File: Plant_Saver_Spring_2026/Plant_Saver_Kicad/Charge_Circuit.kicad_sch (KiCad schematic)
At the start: 16 parts, among them J1 1.25mm, Q1 SSF1341, Q3 SSF1341, Q4 SSF1341, Q5 SSF1341, Q6 SSF1341, Q7 SSF1341, Q8 SSF1341, Q9 SSF1341

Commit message: Sensor Fun
Had to annotate in order to assign footprints, If that messed anything up I'd be happy to fix it. Added a basic 1x4 header for the temp sensor and added the correct female pins/header footprint for the capacitive moisture sensor. Also put a footprint in there for the OLED using the 4pin cable that we don't have but would be nice to. If we choose to go with the headers instead it's and easy change.
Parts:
- CR1: footprint SDO_CFP5_SOD128_NEX -> (none)
- J1: footprint CONN02_530470210_MOL -> (none)
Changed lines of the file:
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@@
 			)
 		)
-		(property "Footprint" "CONN02_530470210_MOL"
+		(property "Footprint" ""
 			(at 185.42 120.65 0)
 			(effects
@@
 			)
 		)
-		(property "Footprint" "SDO_CFP5_SOD128_NEX"
+		(property "Footprint" ""
 			(at 217.17 91.44 0)
 			(effects

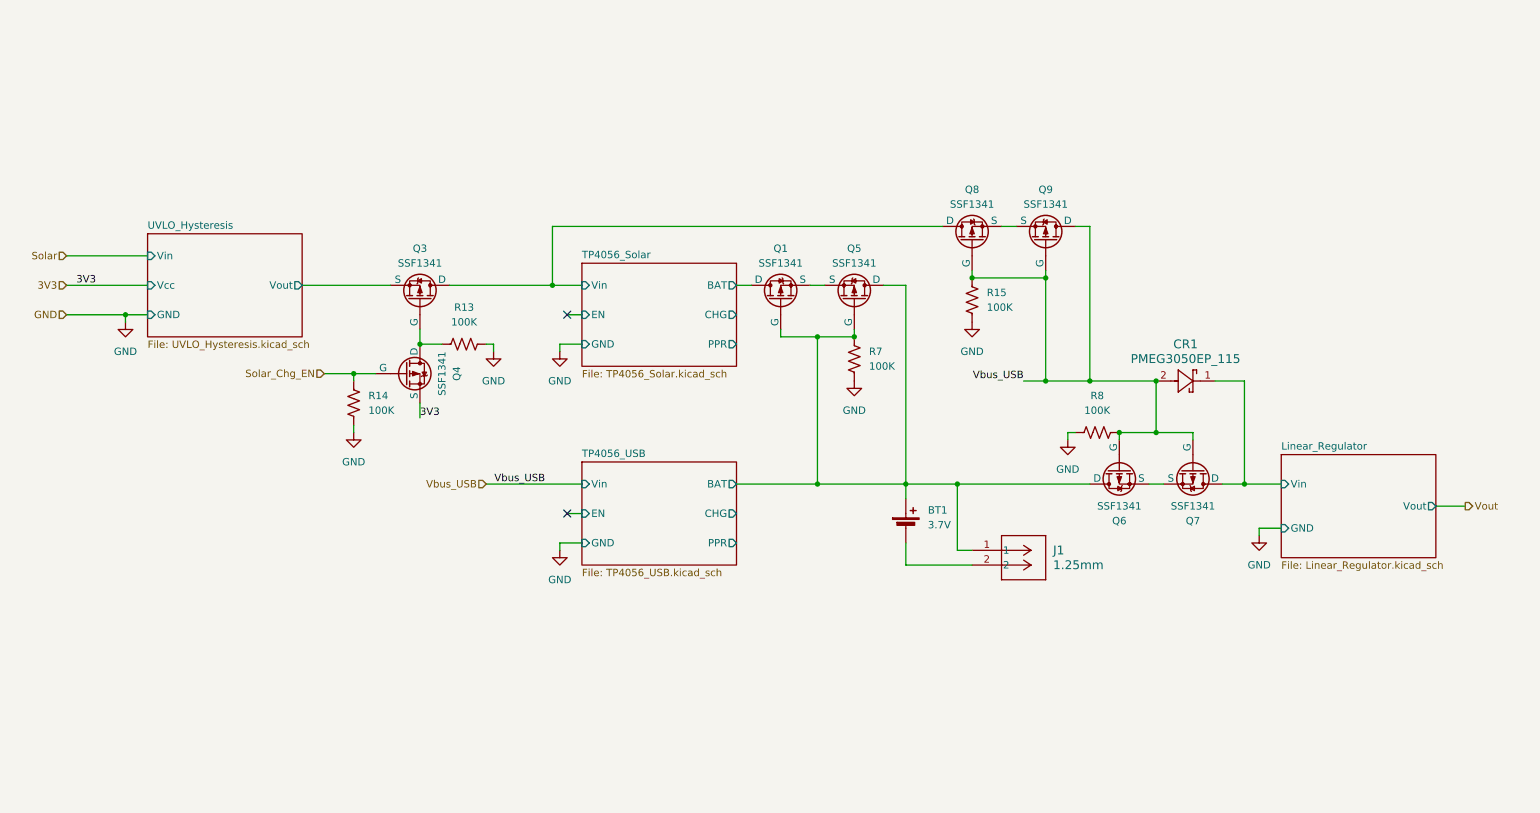
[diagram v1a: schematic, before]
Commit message: Updated Charging Circuit
Replaced TP4056 with MCP73833, replaced schottky diodes
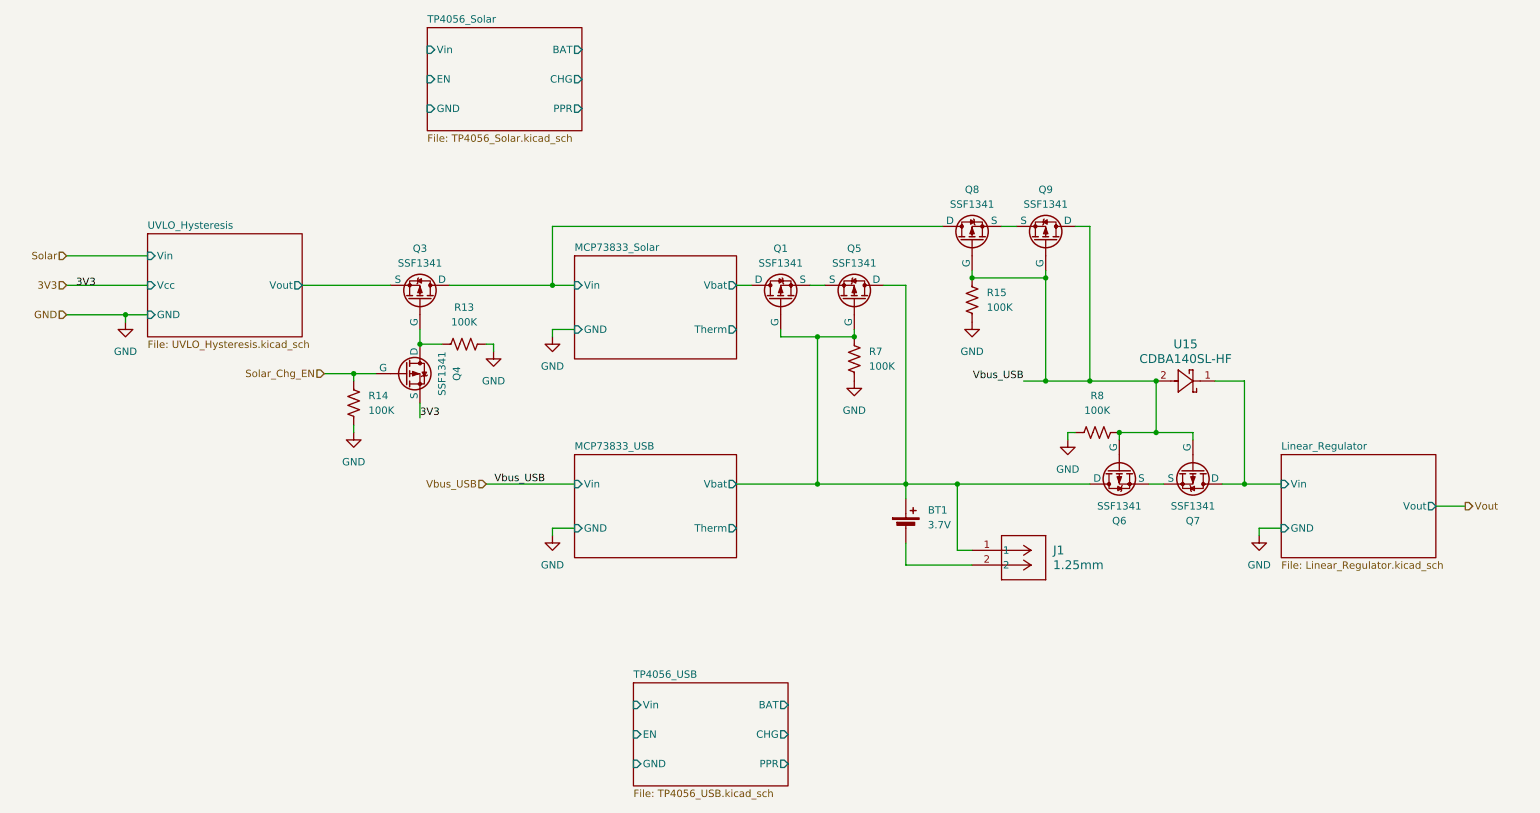
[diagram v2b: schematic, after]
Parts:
- removed CR1: PMEG3050EP_115, symbol PMEG3050EP,115:PMEG3050EP_115
- added U15: CDBA140SL-HF, CDBA-HF, symbol CDBA140SL_HF:CDBA140SL-HF
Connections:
- net Linear_Regulator/Vin: now also U15.1
- net TP4056_Solar/BAT: no longer Q1.1 (D)
- net TP4056_Solar/Vin: no longer Q3.1 (D), Q8.1 (D)
- net TP4056_USB/BAT: no longer BT1.1 (+), J1.1, Q1.2 (G), Q5.1 (D), Q5.2 (G), Q6.1 (D), R7.2
- net Vbus_USB: now also U15.2
- new net MCP73833_Solar/Vbat: Q1.1 (D)
- new net MCP73833_Solar/Vin: Q3.1 (D), Q8.1 (D)
- new net MCP73833_USB/Vbat: BT1.1 (+), J1.1, Q1.2 (G), Q5.1 (D), Q5.2 (G), Q6.1 (D), R7.2
- no-connect marks 2 -> 0
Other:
- added sheet MCP73833_Solar (MCP73833_Solar.kicad_sch)
- added sheet MCP73833_USB (MCP73833_USB.kicad_sch)

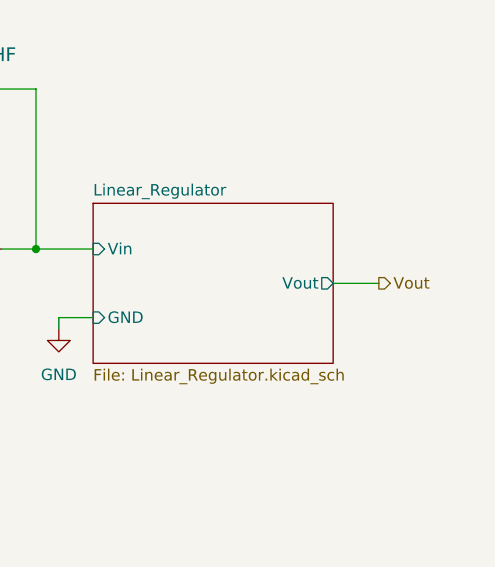
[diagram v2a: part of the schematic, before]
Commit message: Added ESP32 micro and mostly completed its wiring to peripherals
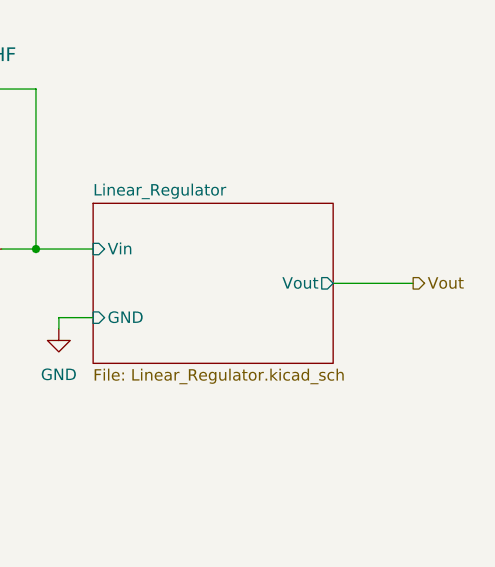
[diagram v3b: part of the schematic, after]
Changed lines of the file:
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@@
 	(wire
 		(pts
-			(xy 265.43 113.03) (xy 270.51 113.03)
+			(xy 265.43 113.03) (xy 274.32 113.03)
 		)
 		(stroke
@@
 	(hierarchical_label "Vout"
 		(shape output)
-		(at 270.51 113.03 0)
+		(at 274.32 113.03 0)
 		(effects
 			(font

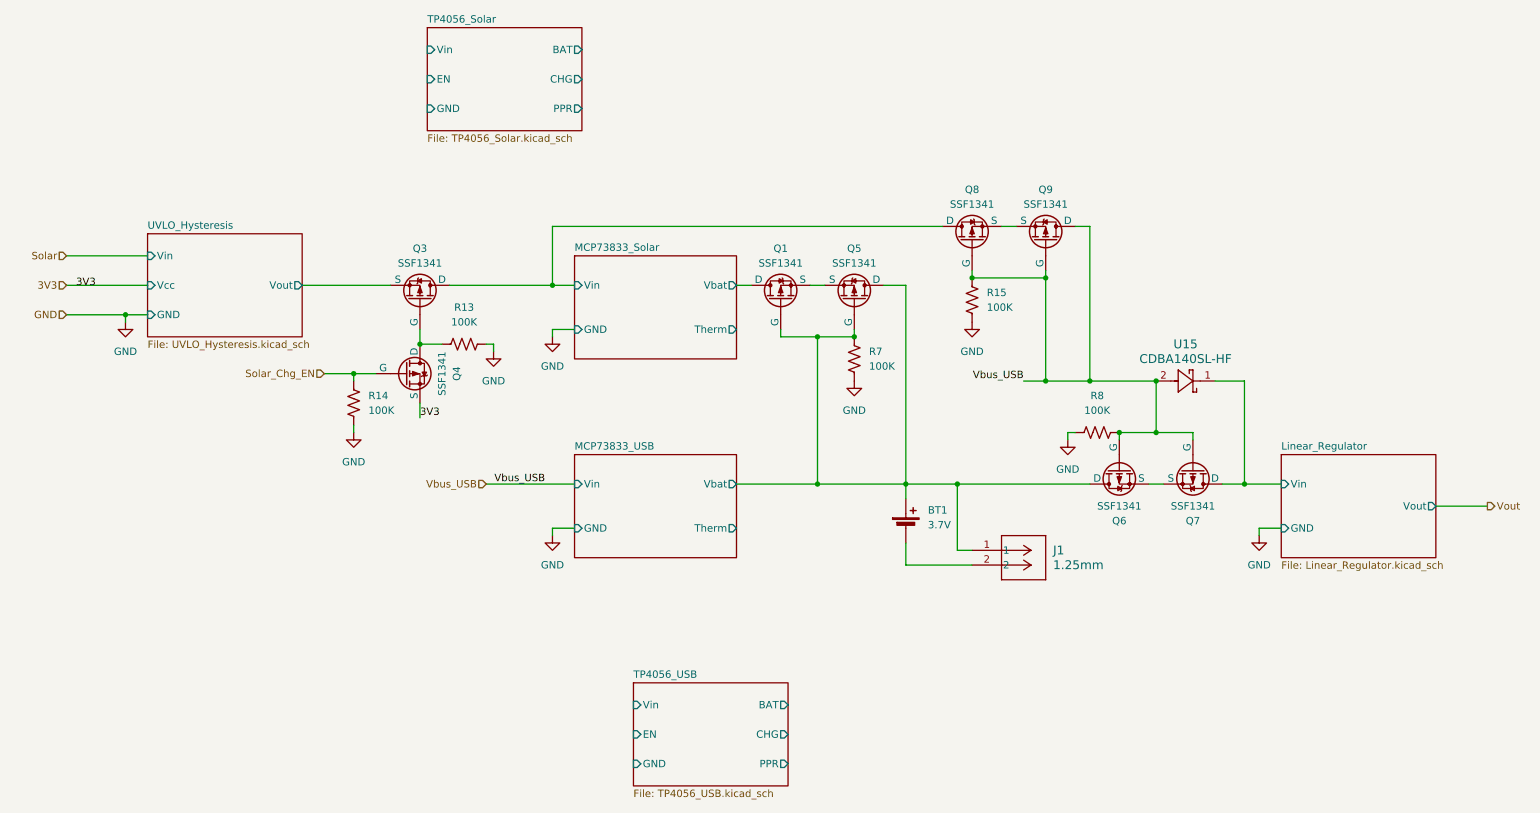
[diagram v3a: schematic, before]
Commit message: Updates to power schematic
Replaced certain selection transistors for lower Rds_on, added thermal cutoff and DW03 for battery protection, swapped in 4-channel op-amps for solar measurement, various misc. improvements.
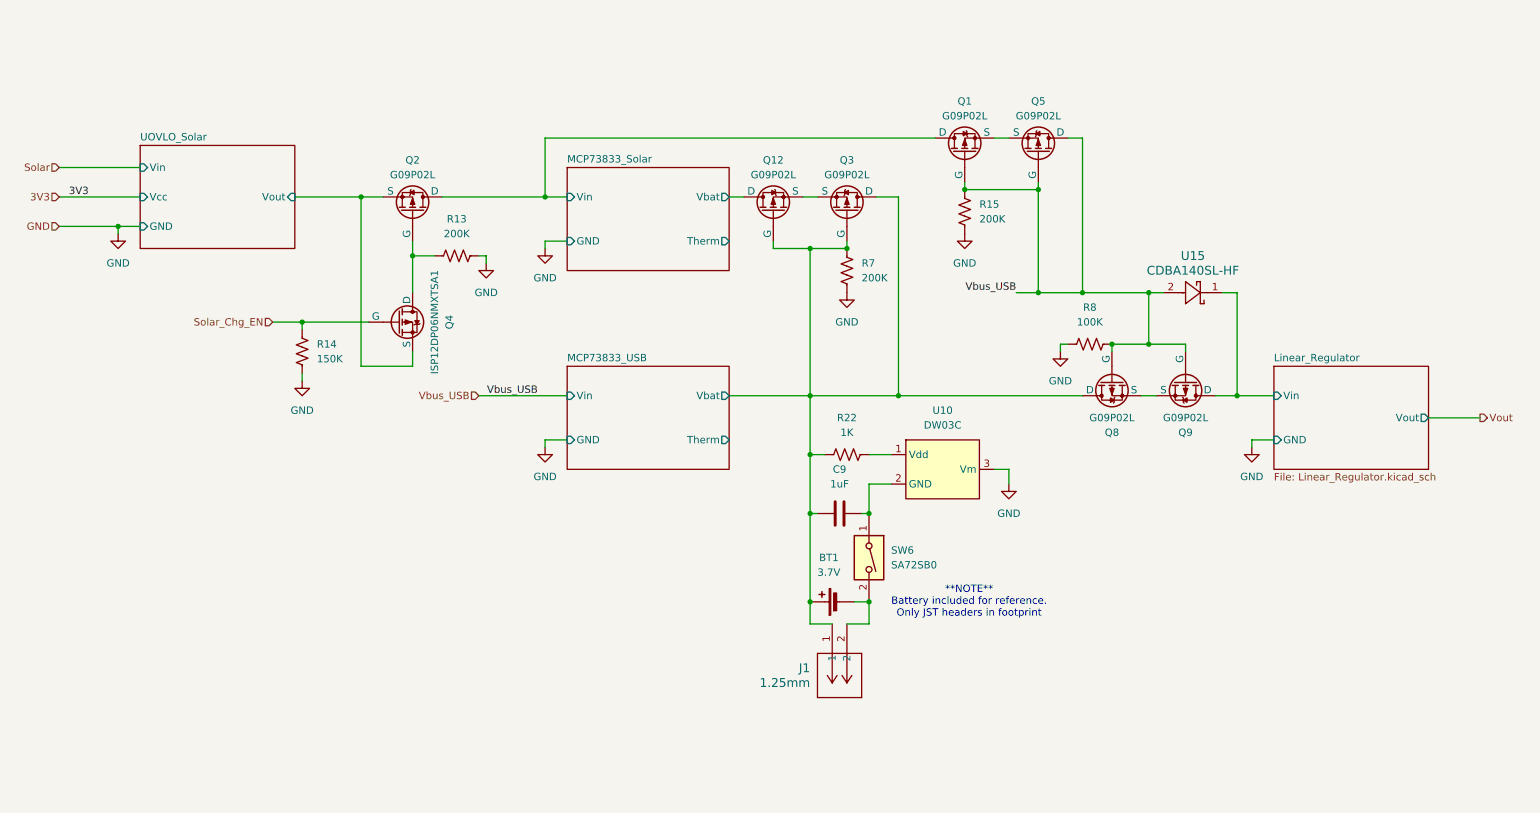
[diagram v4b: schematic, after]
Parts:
- removed Q6, Q7: SSF1341, Package_TO_SOT_SMD:SOT-23_Handsoldering, symbol Simulation_SPICE:PMOS
- added C9: 1uF, C410C105K5R5TA7200:CAP_C410C_AX_X7R_AXIMAX_KEM, symbol Device:C
- added Q12, Q2: G09P02L, G09P02L:TSOT-23, symbol Simulation_SPICE:PMOS
- added R22: 1K, Resistor_THT:R_Axial_DIN0207_L6.3mm_D2.5mm_P10.16mm_Horizontal, symbol Device:R_US
- added SW6: SA72SB0, Resistor_THT:R_Axial_DIN0207_L6.3mm_D2.5mm_P10.16mm_Horizontal, symbol Switch:SW_DIP_x01
- added U10: DW03C, symbol DW03C:_1
- J1: footprint (none) -> 1.25mm Micro-JST Male:CONN02_530470210_MOL
- Q1, Q3, Q5, Q8, Q9: value SSF1341 -> G09P02L; footprint Package_TO_SOT_SMD:SOT-23_Handsoldering -> G09P02L:TSOT-23
- Q4: value SSF1341 -> ISP12DP06NMXTSA1; footprint Package_TO_SOT_SMD:SOT-23_Handsoldering -> ul_ISP12DP06NMXTSA1:PG-SOT223-4_INF
- R13, R15, R7: value 100K -> 200K
- R14: value 100K -> 150K
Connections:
- net 3V3: no longer Q4.3 (S)
- net GND: now also U10.3 (Vm)
- net Linear_Regulator/Vin: now also Q9.1 (D)
- net MCP73833_Solar/Vbat: now also Q12.1 (D); no longer Q1.1 (D)
- net MCP73833_Solar/Vin: now also Q1.1 (D), Q2.1 (D); no longer Q3.1 (D), Q8.1 (D)
- net MCP73833_USB/Vbat: now also Q3.1 (D), Q3.2 (G), Q8.1 (D), C9.1, Q12.2 (G), R22.1; no longer Q1.2 (G), Q5.1 (D), Q5.2 (G)
- net Vbus_USB: now also Q1.2 (G), Q5.1 (D), Q5.2 (G); no longer Q9.1 (D)
- net at Q4.1 (D), R13.1: now also Q2.2 (G); no longer Q3.2 (G)
- net at BT1.2 (-), J1.2: now also SW6.2
- net UVLO_Hysteresis/Vout: no longer names the net of Q3.3 (S)
- net UVLO_Hysteresis/Vout: now also Q12.3 (S)
- new net: R22.2, U10.1 (Vdd)
- new net: C9.2, SW6.1, U10.2 (GND)
- new net UOVLO_Solar/Vout: Q2.3 (S), Q4.3 (S)
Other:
- removed sheet TP4056_Solar
- removed sheet TP4056_USB
- removed sheet UVLO_Hysteresis
- added sheet UOVLO_Solar (UOVLO_Solar.kicad_sch)
- note added: "**NOTE** Battery included for reference. Only JST headers in footprint"
- moved on the sheet: J1, Q4, R13, R14, R15, R7, R8, U15

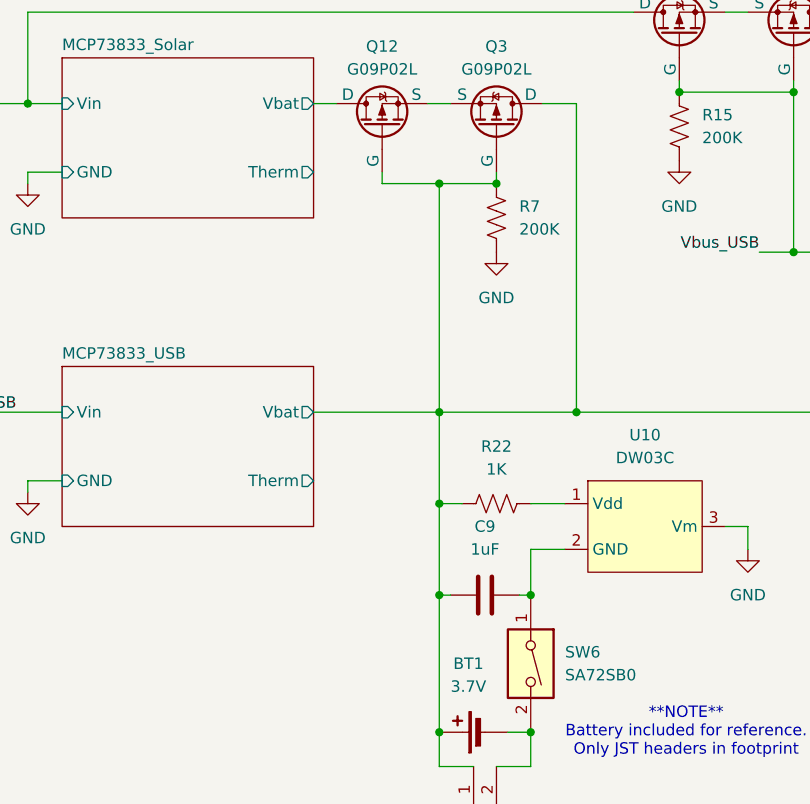
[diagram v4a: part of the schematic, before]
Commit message: Schematic updates
Added USB charge LEDs, updated PMOS gates, added micro connections and revised some of the charging set up.
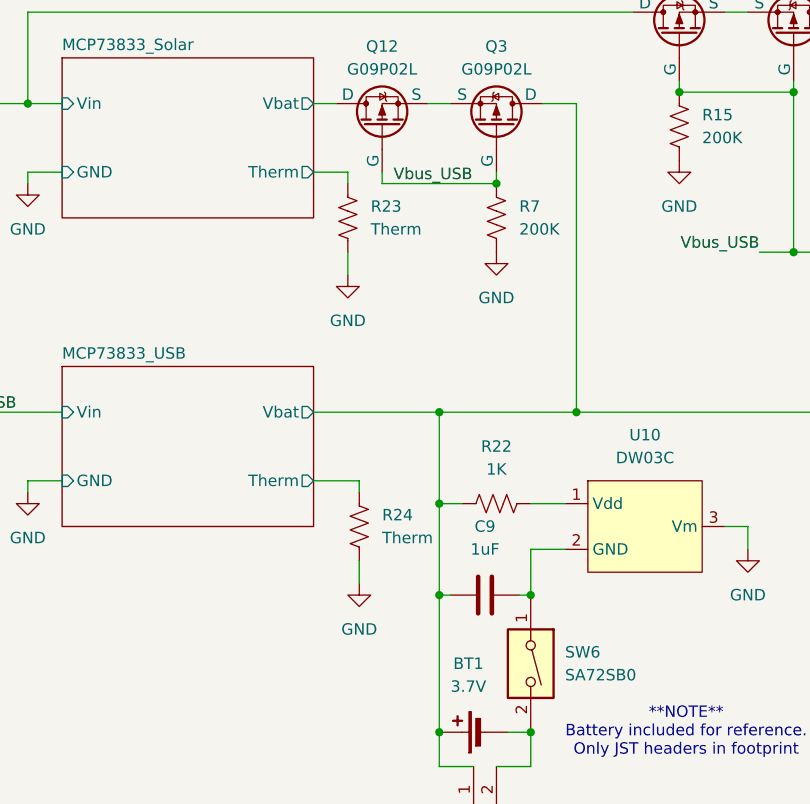
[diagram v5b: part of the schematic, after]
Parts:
- added R23, R24: Therm, Resistor_THT:R_Axial_DIN0207_L6.3mm_D2.5mm_P10.16mm_Horizontal, symbol Device:R_US
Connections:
- net GND: now also R23.1, R24.1
- net MCP73833_Solar/Therm: now also R23.2
- net MCP73833_USB/Therm: now also R24.2
- net MCP73833_USB/Vbat: no longer Q12.2 (G), Q3.2 (G), R7.2
- net Vbus_USB: now also Q12.2 (G), Q3.2 (G), R7.2

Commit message: Minor updates to charge/power
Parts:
- added U11: CDBA140SL-HF, CDBA-HF, symbol CDBA140SL_HF:CDBA140SL-HF
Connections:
- net Vbus_USB: now also U11.2; no longer Q5.1 (D), Q8.2 (G), Q9.2 (G), R8.1, U15.2
- new net: Q5.1 (D), Q8.2 (G), Q9.2 (G), R8.1, U11.1, U15.2
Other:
- moved on the sheet: BT1, C9, J1, Q8, Q9, R22, R24, R8, SW6, U10, U15
